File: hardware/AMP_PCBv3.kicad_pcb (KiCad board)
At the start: 2 copper layers, 70 x 82.5 mm, 84 parts, among them CN10 Male_R2, CN7 Male_L1, J1 Input_PWR, J2 USB_B_Mini, J3 LED_Header, J4 VESC_PPM, J5 VESC_COMM, J6 STEERING, M1 Brake, M2 Fan_PC_3pin, M3 Fan_PC_3pin, M4 Fan_PC_3pin, M5 Fan_PC_3pin, Q1 DMN2310U, Q2 DMN2310U, Q3 DMN2310U, Q4 DMN2310U, U1 TPS56624x, U2 RFM95W-915S2, U3 FT230XS, U4 VNH5200A-E, U5 ICM-20948, U6 USBLC6-2SC6, U7 TLV74318P

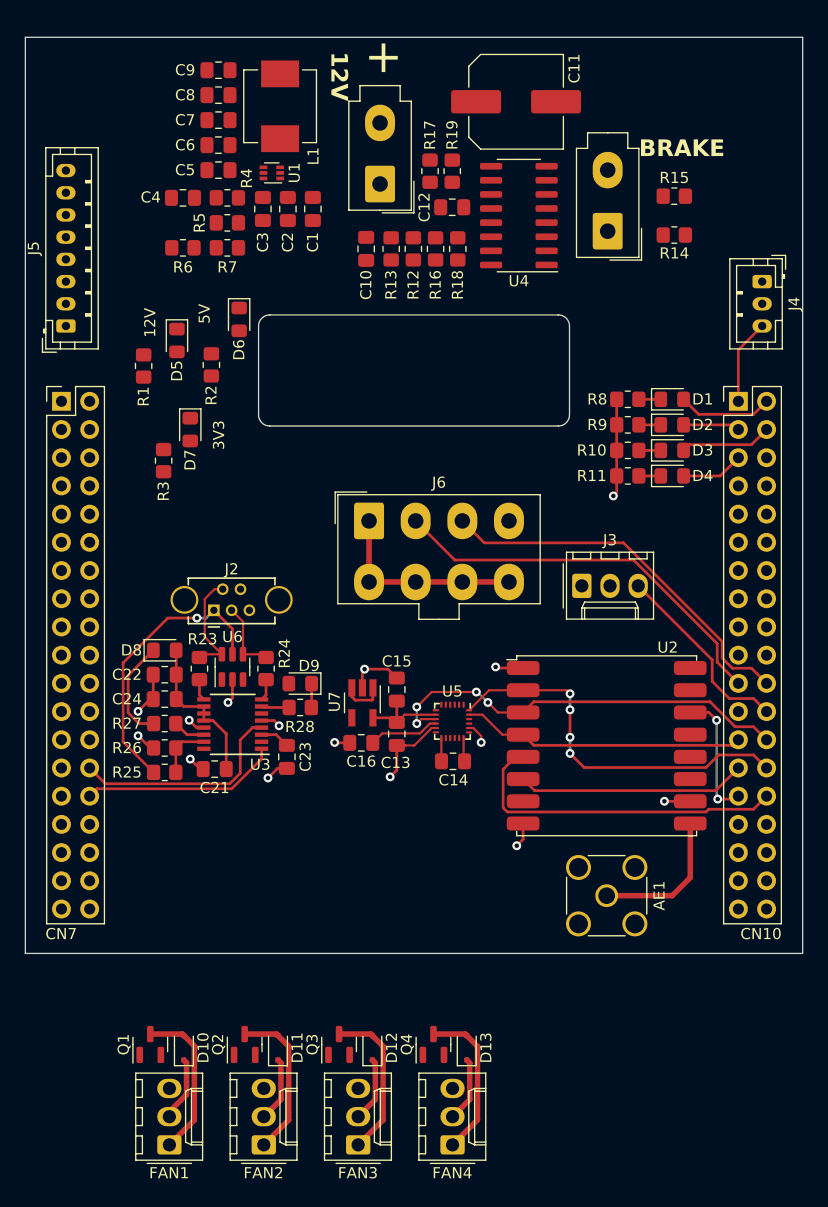
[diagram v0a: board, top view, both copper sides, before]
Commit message: Add level shifters
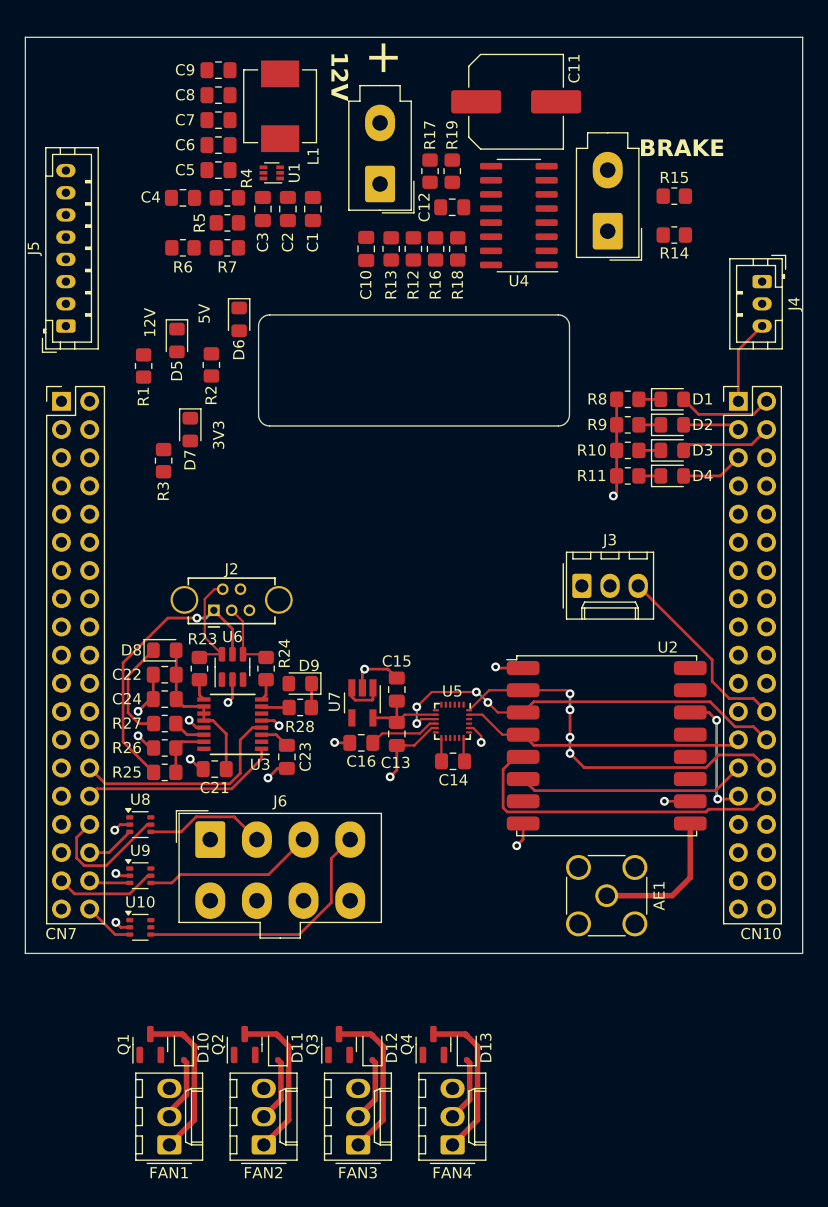
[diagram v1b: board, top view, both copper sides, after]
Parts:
- added U10: SN74LVC1T45DCK, Package_TO_SOT_SMD:SOT-363_SC-70-6, F.Cu at (119.1, 123.7)
- added U8: SN74LVC1T45DCK, Package_TO_SOT_SMD:SOT-363_SC-70-6, F.Cu at (119.1, 114.4)
- added U9: SN74LVC1T45DCK, Package_TO_SOT_SMD:SOT-363_SC-70-6, F.Cu at (119.1, 119.0)
- moved J6 32.1 mm to (125.4, 115.8)
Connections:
- J6 pad 2: /PA9 -> /STEERING_INPUT_B+
- J6 pad 3: /PB2 -> /STEERING_INPUT_A+
- J6 pad 4: +12V -> /STEERING_ENABLE+
- Q1 pad 1: /PC2 -> unconnected-(Q1-G-Pad1)
- Q2 pad 1: /PC1 -> unconnected-(Q2-G-Pad1)
- Q3 pad 1: /PC0 -> unconnected-(Q3-G-Pad1)
- Q4 pad 1: /PC3 -> unconnected-(Q4-G-Pad1)
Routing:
- net /PA9: track 36.1 -> 0.00 mm
- net /PB2: track 34.3 -> 0.00 mm
- net /STEERING_ENABLE+: track 0.00 -> 23.8 mm
- net /STEERING_INPUT_A+: track 0.00 -> 15.4 mm
- net GND: track 66.8 -> 53.0 mm, vias 15 -> 18
- net /PA4: track 0.00 -> 12.0 mm
- net /STEERING_INPUT_B+: track 0.00 -> 11.0 mm
- net /PC2: track 0.00 -> 9.21 mm
- net /PC0: track 0.00 -> 4.56 mm
- net /PB0: track 0.00 -> 4.38 mm
- net /PC1: track 0.00 -> 3.69 mm

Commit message: Place and route
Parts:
- removed C3, C9: 100nF, Capacitor_SMD:C_0805_2012Metric_Pad1.18x1.45mm_HandSolder
- removed C8: 22uF, Capacitor_SMD:C_0805_2012Metric_Pad1.18x1.45mm_HandSolder
- removed R18, R19: 3.3k, Resistor_SMD:R_0805_2012Metric_Pad1.20x1.40mm_HandSolder
- C11: footprint Capacitor_SMD:C_Elec_8x10.2 -> Capacitor_THT:CP_Radial_D8.0mm_P3.50mm
- C2: value 10uF -> 2.7nF
- C4: value 33pF -> 100nF
- L1: value 2.2uH -> 3.6uH; footprint Inductor_SMD:L_Vishay_IHLP-2525 -> Inductor_SMD:L_Changjiang_FNR8040S
- R4: value 100k -> 200k
- R6: value 220k -> 115k
- R7: value 30k -> 22.1k
- U1: value TPS56624x -> AP64500; footprint Package_TO_SOT_SMD:SOT-563 -> Package_SO:Diodes_SO-8EP
- U4: value VNH5200A-E -> VNH7070AS
- moved M5 89.3 mm to (119.8, 58.3), turned to 0 degrees
- moved D13 76.2 mm to (120.4, 63.7), turned to -90 degrees
- moved M4 74.9 mm to (119.8, 70.8), turned to 0 degrees
- moved Q4 73.6 mm to (123.4, 64.0), turned to -90 degrees
- moved D12 61.5 mm to (120.4, 76.2), turned to -90 degrees
- moved M3 60.8 mm to (119.8, 83.3), turned to 0 degrees
- moved M2 60.5 mm to (129.8, 83.3), turned to 0 degrees
- moved Q3 59.3 mm to (123.4, 76.5), turned to -90 degrees
- moved Q1 47.2 mm to (133.5, 89.0), turned to -90 degrees
- moved D11 47.1 mm to (120.4, 88.7), turned to -90 degrees
- moved D10 46.4 mm to (130.4, 88.7), turned to -90 degrees
- moved Q2 45.5 mm to (123.4, 89.0), turned to -90 degrees
- moved R3 32.2 mm to (113.7, 50.3), turned to 180 degrees
- moved D7 29.1 mm to (117.7, 50.3), turned to 0 degrees
- moved R1 28.0 mm to (113.7, 45.7), turned to 180 degrees
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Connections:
- C2 pad 1: +12V -> Net-(C2-Pad1)
- C4 pad 1: /E5V -> Net-(U1-BST)
- C4 pad 2: Net-(U1-FB) -> Net-(U1-SW)
- CN10 pad 13: /BRAKE_INB -> /PA6
- CN10 pad 15: /BRAKE_INA -> /PA7
- CN10 pad 16: /BRAKE_ENA -> /PB12
- CN10 pad 19: /BRAKE_CS -> /PC7
- CN10 pad 2: /PC8 -> /BRAKE_INA
- CN10 pad 3: /PB8 -> /BRAKE_SEL0
- CN10 pad 4: /PC6 -> /BRAKE_INB
- CN10 pad 5: /PB9 -> /BRAKE_PWM
- CN10 pad 6: /BRAKE_ENB -> /BRAKE_CS
- D1 pad 2: /PC8 -> /PA12
- D2 pad 2: /PB8 -> /PA5
- D3 pad 2: /PC6 -> /PA11
- D4 pad 2: /PB9 -> /PB12
- J3 pad 2: +5V -> /E5V
- Q1 pad 1: unconnected-(Q1-G-Pad1) -> /PA15
- Q2 pad 1: unconnected-(Q2-G-Pad1) -> /PB7
- Q3 pad 1: unconnected-(Q3-G-Pad1) -> /PC11
- Q4 pad 1: unconnected-(Q4-G-Pad1) -> /PC10
- R16 pad 1: /BRAKE_ENA -> /BRAKE_SEL0
- R17 pad 2: /BRAKE_ENB -> /BRAKE_PWM
- R4 pad 1: +12V -> GND
- R4 pad 2: Net-(U1-EN) -> Net-(U1-RT/CLK)
- R5 pad 1: Net-(U1-EN) -> Net-(C2-Pad1)
- R5 pad 2: GND -> Net-(U1-COMP)
- U1 pad 1: +12V -> Net-(U1-BST)
- U1 pad 2: Net-(U1-SW) -> +12V
- U1 pad 3: GND -> +12V
- U1 pad 4: GND -> Net-(U1-RT/CLK)
- U1 pad 5: Net-(U1-EN) -> Net-(U1-FB)
- U1 pad 6: Net-(U1-FB) -> Net-(U1-COMP)
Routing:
- net +3V3: track 20.7 -> 189.7 mm, vias 0 -> 11
- net /E5V: track 0.00 -> 138.5 mm
- net +12V: track 23.4 -> 158.9 mm, vias 0 -> 2
- net +5V: track 0.00 -> 85.3 mm, vias 0 -> 11
- net GND: track 53.0 -> 109.5 mm, vias 18 -> 33
- net /BRAKE_CS: track 0.00 -> 40.9 mm
- net /BRAKE_PWM: track 0.00 -> 40.6 mm
- net /IMU_INT1: track 0.00 -> 40.4 mm, vias 0 -> 2
- net /IMU_CS: track 0.00 -> 35.1 mm, vias 0 -> 2
- net /PA15: track 0.00 -> 33.2 mm, vias 0 -> 2
- net /PB7: track 0.00 -> 31.8 mm, vias 0 -> 2
- net /BRAKE_SEL0: track 0.00 -> 30.1 mm
- net /PB12: track 0.00 -> 24.8 mm
- net /PC10: track 0.00 -> 23.3 mm, vias 0 -> 2
- net /BRAKE_INB: track 0.00 -> 23.2 mm
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- added copper zone on F.Cu, net /E5V
- added copper zone on B.Cu, net GND
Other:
- outline, holes or cut-outs redrawn
- board text added: "JETSON"
- board text added: "LED"
- board text added: "STEERING"
- board text added: "VESC COMM"
- board text added: "VESC PPM"

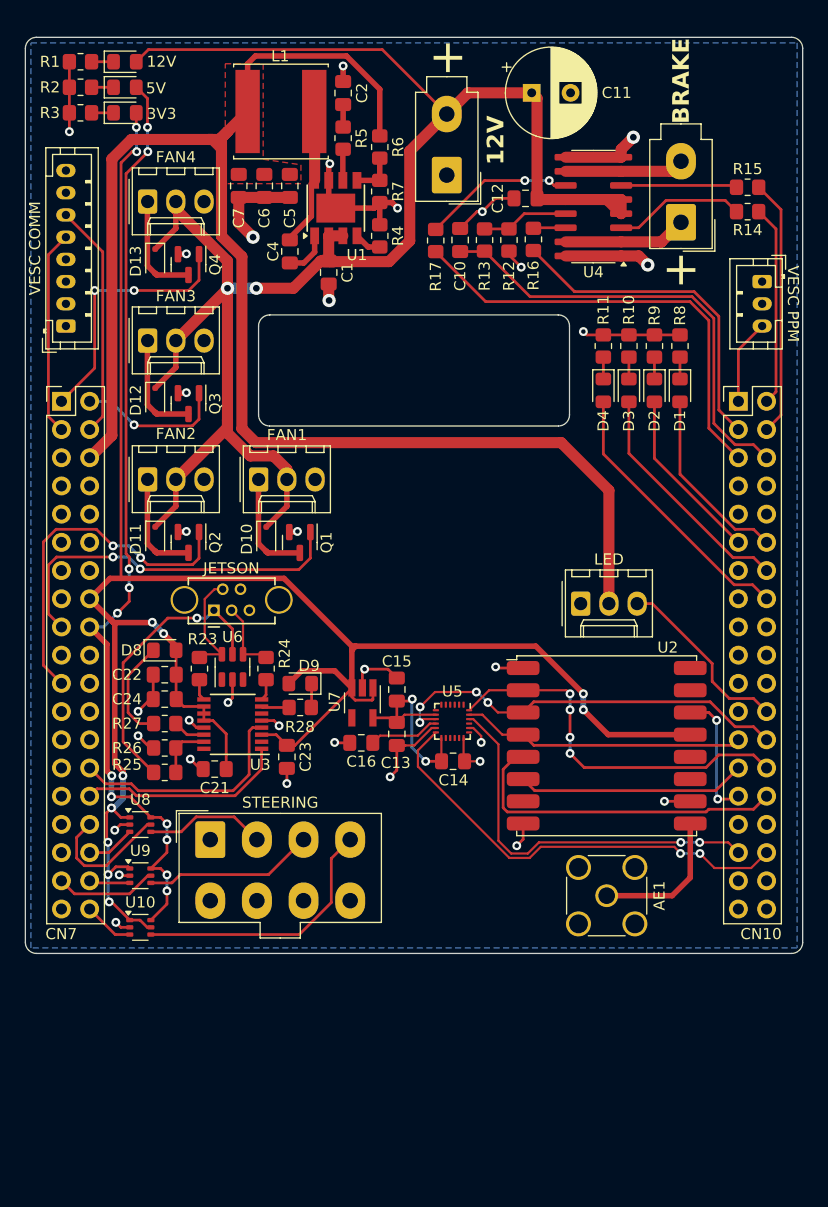
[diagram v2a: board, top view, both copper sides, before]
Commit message: Add level shifter for LEDs
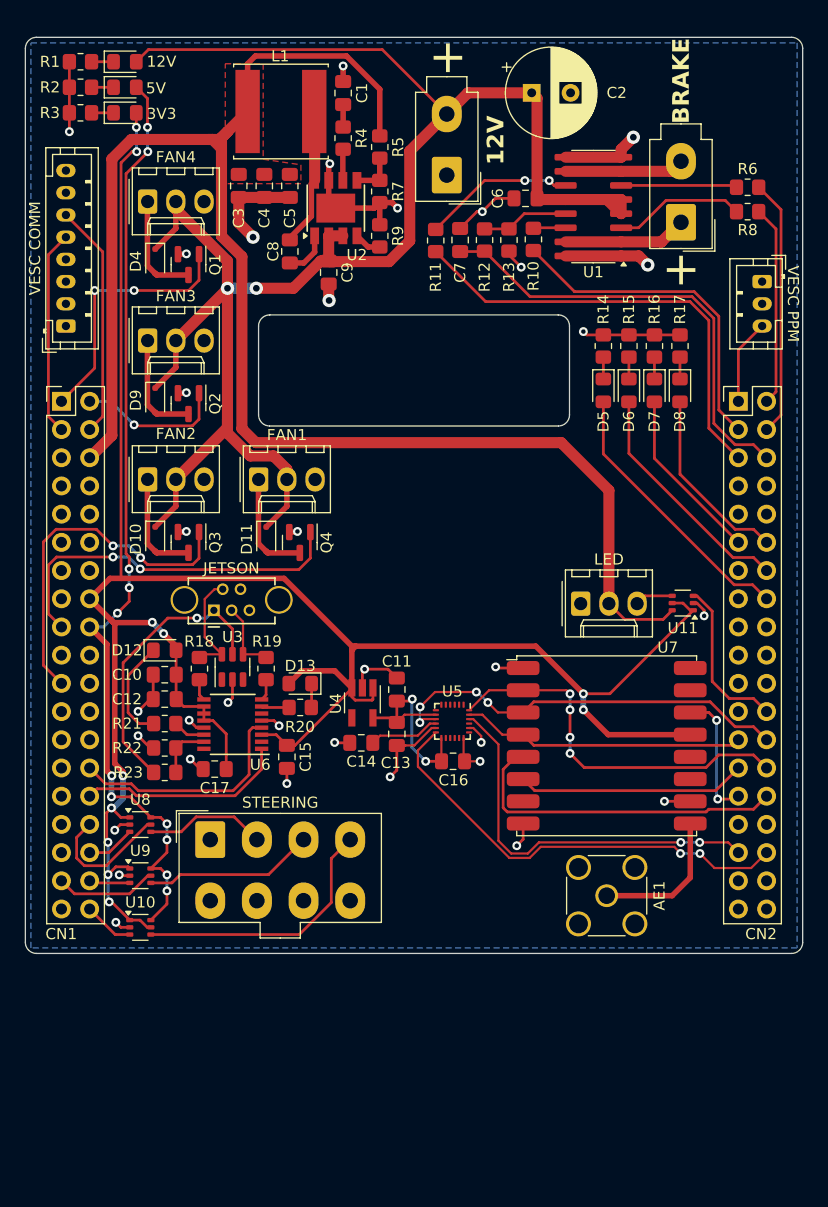
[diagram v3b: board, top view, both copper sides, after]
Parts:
- added U11: SN74LVC1T45DCK, Package_TO_SOT_SMD:SOT-363_SC-70-6, F.Cu at (167.9, 94.5)
- renumbered C2 to C1, C22 to C10, C15 to C11, C24 to C12, C16 to C14, C23 to C15, C14 to C16, C21 to C17, C11 to C2, C7 to C3, C6 to C4, C12 to C6, C10 to C7, C4 to C8, C1 to C9, CN7 to CN1, CN10 to CN2, D5 to D1, D11 to D10, D10 to D11, D8 to D12, D9 to D13, D6 to D2, D7 to D3, D13 to D4, D4 to D5, D3 to D6, D2 to D7, D1 to D8, D12 to D9, J4 to J2, J5 to J3, J3 to J4, J2 to J5, M5 to M1, M1 to M2, M4 to M3, M3 to M4, M2 to M5, Q4 to Q1, Q3 to Q2, Q2 to Q3, Q1 to Q4, R16 to R10, R17 to R11, R13 to R12, R12 to R13, R11 to R14, R10 to R15, R9 to R16, R8 to R17, R23 to R18, R24 to R19, R28 to R20, R27 to R21, R26 to R22, R25 to R23, R5 to R4, R6 to R5, R15 to R6, R14 to R8, R4 to R9, U4 to U1, U1 to U2, U6 to U3, U7 to U4, U3 to U6, U2 to U7
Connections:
- J4 pad 3: /LED_SIG -> /LED_SIG_5V
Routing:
- net +3V3: track 189.7 -> 204.9 mm
- net /E5V: track 138.5 -> 145.1 mm
- net /LED_SIG_5V: track 0.00 -> 3.45 mm
- net /LED_SIG: track 16.6 -> 14.6 mm
- net GND: track 109.5 -> 111.3 mm, vias 33 -> 34

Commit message: JLC assembly parts
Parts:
- L1: footprint Inductor_SMD:L_Changjiang_FNR8040S -> Inductor_SMD:L_Bourns-SRN8040_8x8.15mm
- R14, R15, R16, R17, R3: value 260 -> 300
- R2: value 600 -> 470
- R20, R21: value 270 -> 300
- moved L1 0.17 mm to (131.6, 50.2)
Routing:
- net /E5V: track 145.1 -> 144.1 mm
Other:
- board text added: "ERR/STAT4"
- board text added: "STAT1"
- board text added: "STAT2"
- board text added: "STAT3"

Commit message: Schematic cleanup
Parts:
- removed CN1: Male_L1, Connector_PinHeader_2.54mm:PinHeader_2x19_P2.54mm_Vertical
- removed CN2: Male_R2, Connector_PinHeader_2.54mm:PinHeader_2x19_P2.54mm_Vertical
- added U12: ~, AMP_Custom:NUCLEO64, F.Cu at (143.8, 78.5)
- D5: value STAT4 -> STAT1
- D6: value STAT3 -> STAT2
- D7: value STAT2 -> STAT3
- D8: value STAT1 -> STAT4
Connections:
- net /E5V renamed +5P
- net /LED_SIG_5V renamed /Status LEDs/LED_SIG_5V
- net /PB10 renamed /SPI2_SCK
- net /PB14 renamed /SPI2_MISO
- net /PB15 renamed /SPI2_MOSI
- net Net-(M2-+) renamed /Brake Controller/OUT_A
- net Net-(M2--) renamed /Brake Controller/OUT_B
- D5 pad 2: /PB12 -> /STAT1
- D6 pad 2: /PA11 -> /STAT2
- D7 pad 2: /PA5 -> /STAT3
- D8 pad 2: /PA12 -> /STAT4
- J2 pad 3: /PC9 -> /VESC_SERVO
- J3 pad 5: /PC12 -> /UART5_TX
- J3 pad 6: /PD2 -> /UART5_RX
- Q1 pad 1: /PC10 -> /FAN1
- Q2 pad 1: /PC11 -> /FAN2
- Q3 pad 1: /PB7 -> /FAN3
- Q4 pad 1: /PA15 -> /FAN4
- U10 pad 3: /PC0 -> /STEERING_ENABLE+_3V3
- U6 pad 1: /PA1 -> /UART4_RX
- U6 pad 4: /PA0 -> /UART4_TX
- U7 pad 14: /PB5 -> /LORA_DIO0
- U7 pad 5: /PB13 -> /LORA_NSS
- U7 pad 6: /PB4 -> /LORA_RST
- U8 pad 3: /PB0 -> /STEERING_INPUT_B+_3V3
- U8 pad 5: /PA4 -> /STEERING_INPUT_B+_DIR
- U9 pad 3: /PC1 -> /STEERING_INPUT_A+_3V3
- U9 pad 5: /PC2 -> /STEERING_INPUT_A+_DIR
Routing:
- net /PA15: track 33.2 -> 0.00 mm, vias 2 -> 0
- net /FAN4: track 0.00 -> 33.2 mm, vias 0 -> 2
- net /PB7: track 31.8 -> 0.00 mm, vias 2 -> 0
- net /FAN3: track 0.00 -> 31.8 mm, vias 0 -> 2
- net /PB13: track 30.2 -> 0.00 mm
- net /LORA_NSS: track 0.00 -> 30.2 mm
- net /STAT1: track 0.00 -> 24.8 mm
- net /PB12: track 24.8 -> 0.00 mm
- net /PC10: track 23.3 -> 0.00 mm, vias 2 -> 0
- net /FAN1: track 0.00 -> 23.3 mm, vias 0 -> 2
- net /STAT2: track 0.00 -> 21.4 mm
- net /PA11: track 21.4 -> 0.00 mm
- net /UART5_RX: track 0.00 -> 21.2 mm
- net /PD2: track 21.2 -> 0.00 mm
- net /UART4_TX: track 0.00 -> 21.0 mm
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
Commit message: Final touches for assembly
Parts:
- added G***: LOGO, AMP_Custom:Logo, F.Cu at (146.8, 88.4)
- added H1: Tooling Hole, AMP_Custom:JLCPCB_Tooling_Hole, F.Cu at (123.8, 48.5)
- added H2: Tooling Hole, AMP_Custom:JLCPCB_Tooling_Hole, F.Cu at (173.8, 48.5)
- added H3: Tooling Hole, AMP_Custom:JLCPCB_Tooling_Hole, F.Cu at (168.8, 123.5)
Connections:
- net +5P renamed E5V
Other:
- board text added: "AMP PCBv3 Revision B"
- board text added: "JLCJLCJLCJLC"

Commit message: Update revision
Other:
- board text added: "AMP PCBv3 Revision ${REVISION}"
- board text removed: "AMP PCBv3 Revision B"
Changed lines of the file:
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@@
 	(title_block
 		(title "AMP PCBv3")
-		(date "2024-04-03")
-		(rev "B")
+		(date "2024-04-14")
+		(rev "C")
 		(company "Autonomous Motorsports Purdue")
 	)
@@
 		)
 	)
-	(gr_text "AMP PCBv3\nRevision B"
+	(gr_text "AMP PCBv3\nRevision ${REVISION}"
 		(at 142.85 123 0)
 		(layer "F.SilkS")

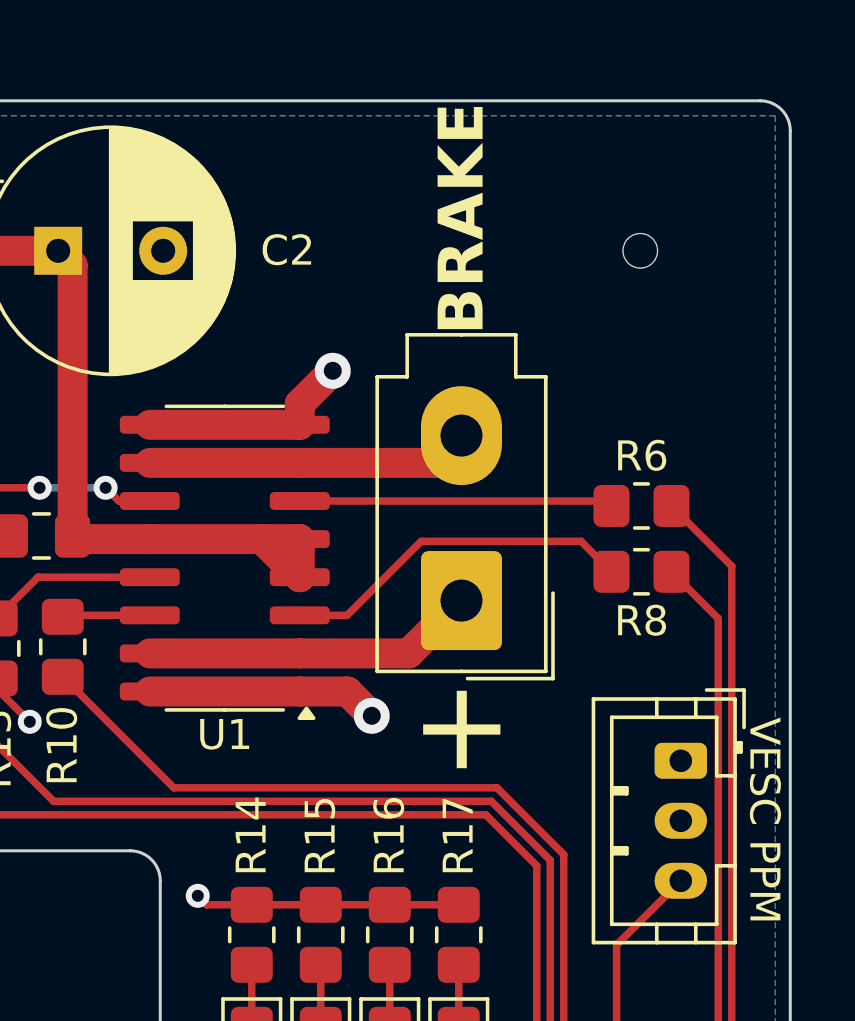
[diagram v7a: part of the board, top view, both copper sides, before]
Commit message: Fix #10
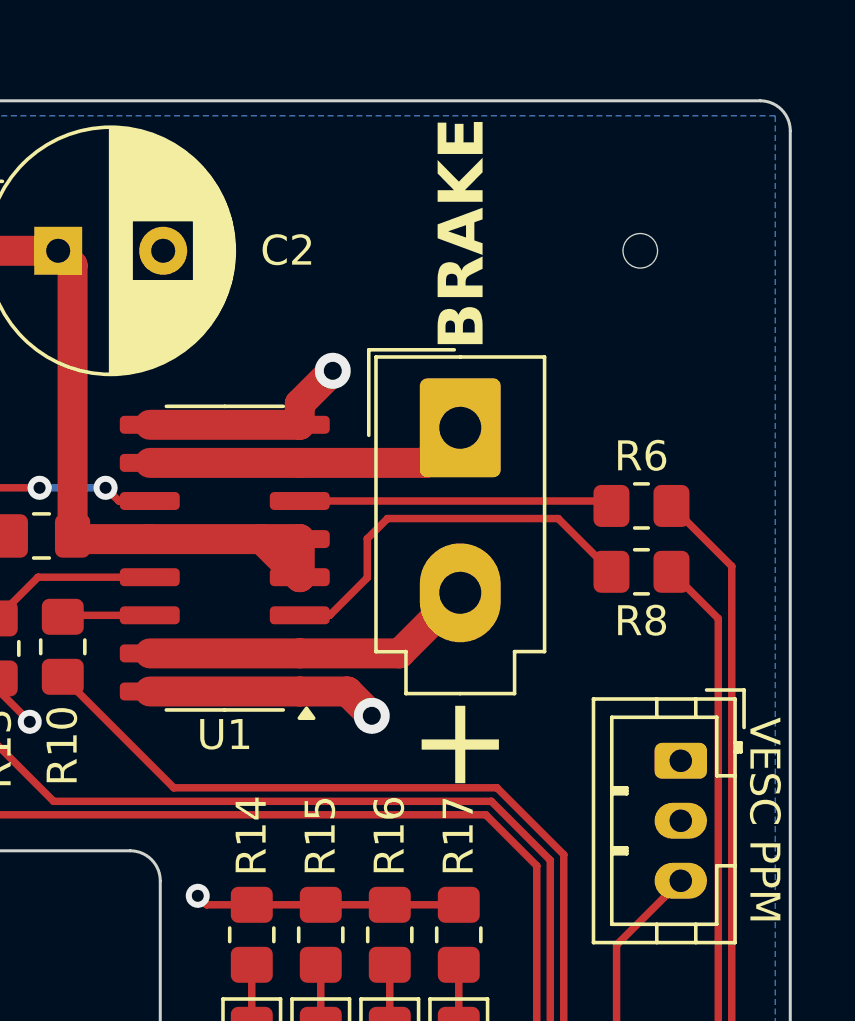
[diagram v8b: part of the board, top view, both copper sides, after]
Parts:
- moved M2 5.76 mm to (167.8, 54.4), turned to 0 degrees
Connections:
- M2 pad 1: /Brake Controller/OUT_A -> /Brake Controller/OUT_B
- M2 pad 2: /Brake Controller/OUT_B -> /Brake Controller/OUT_A
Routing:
- net Net-(U1-INA): track 11.8 -> 13.2 mm
- net /Brake Controller/OUT_A: track 11.1 -> 12.0 mm
